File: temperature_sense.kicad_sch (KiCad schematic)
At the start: 1 part, among them U1 BQ79616PAPRQ1

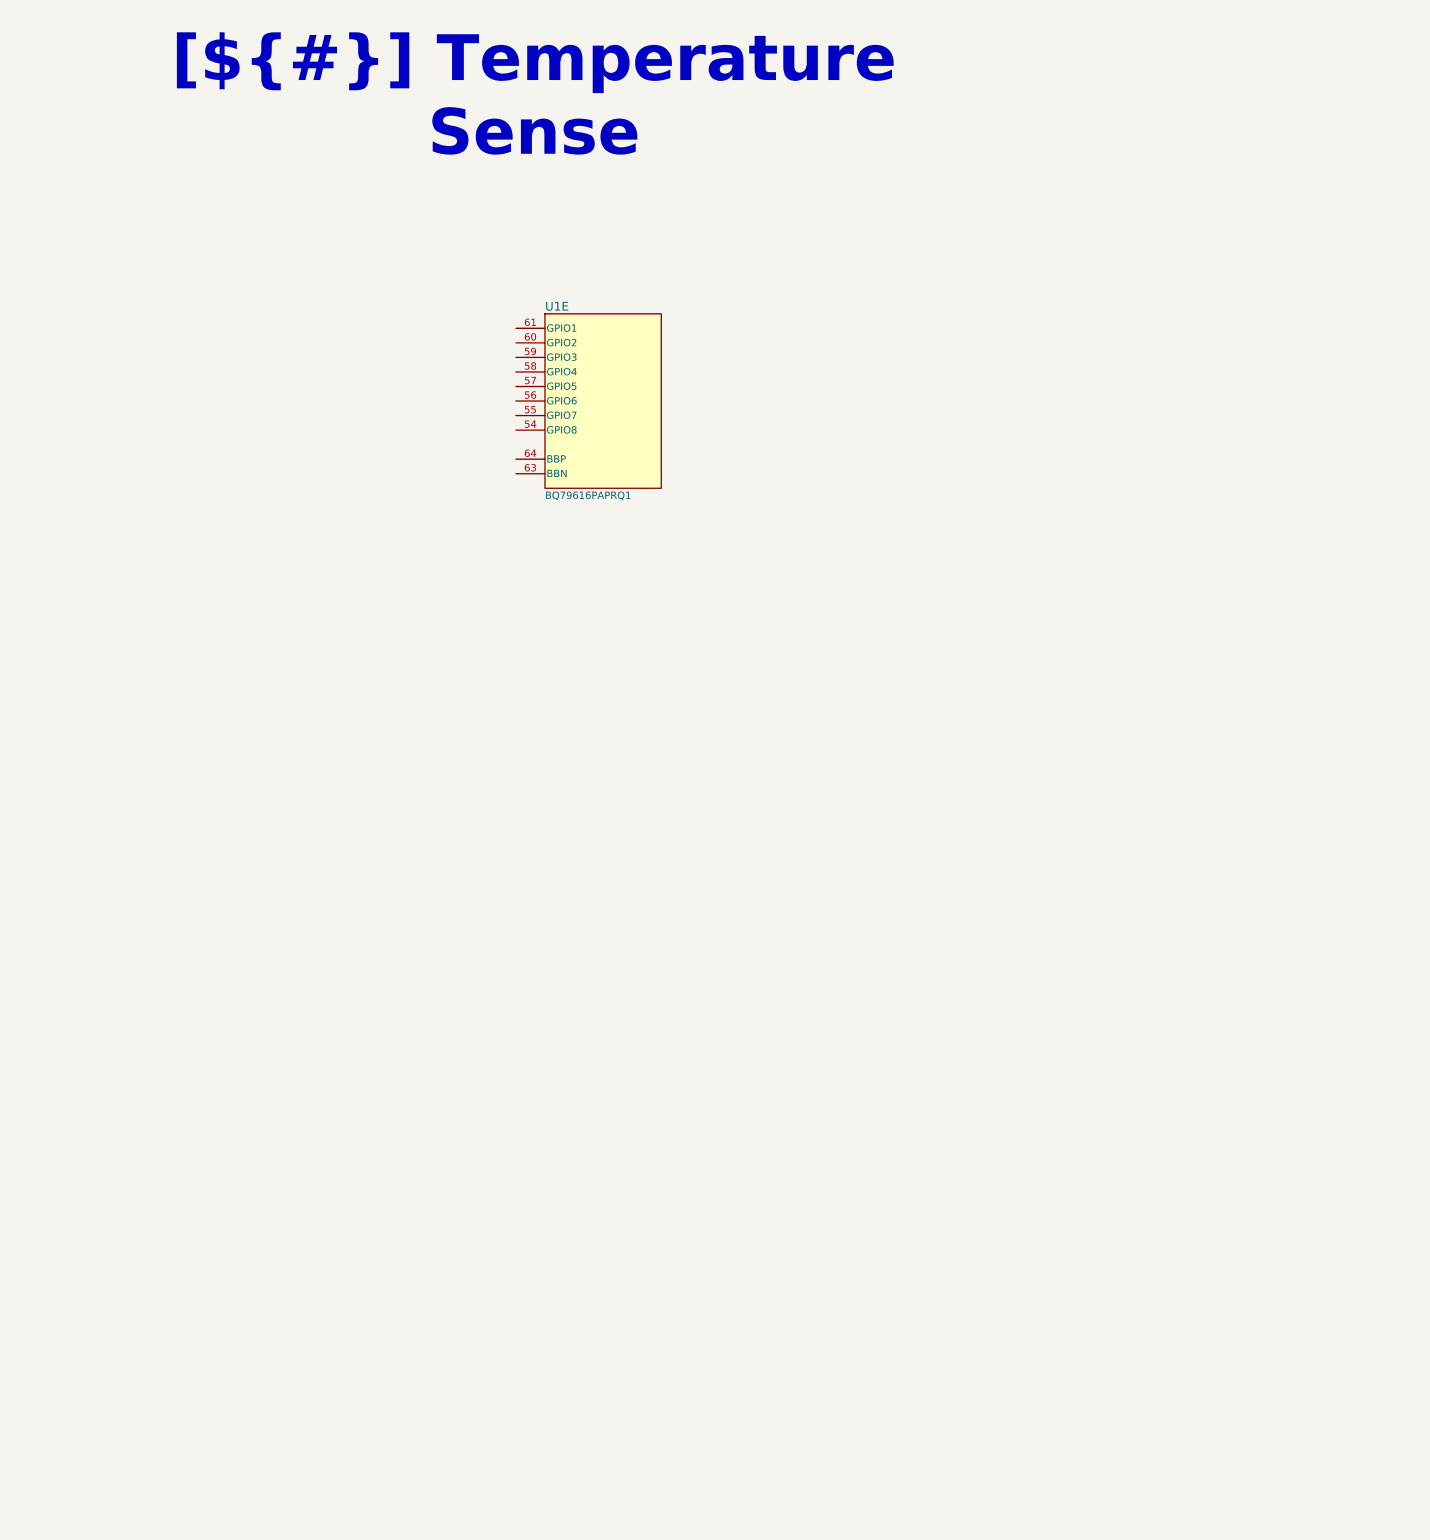
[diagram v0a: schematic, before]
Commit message: SCH:[Hiarchy, Temp, Power]:Inital schmatics of temp, balance, power mostly there need to add design notes and layout notes.
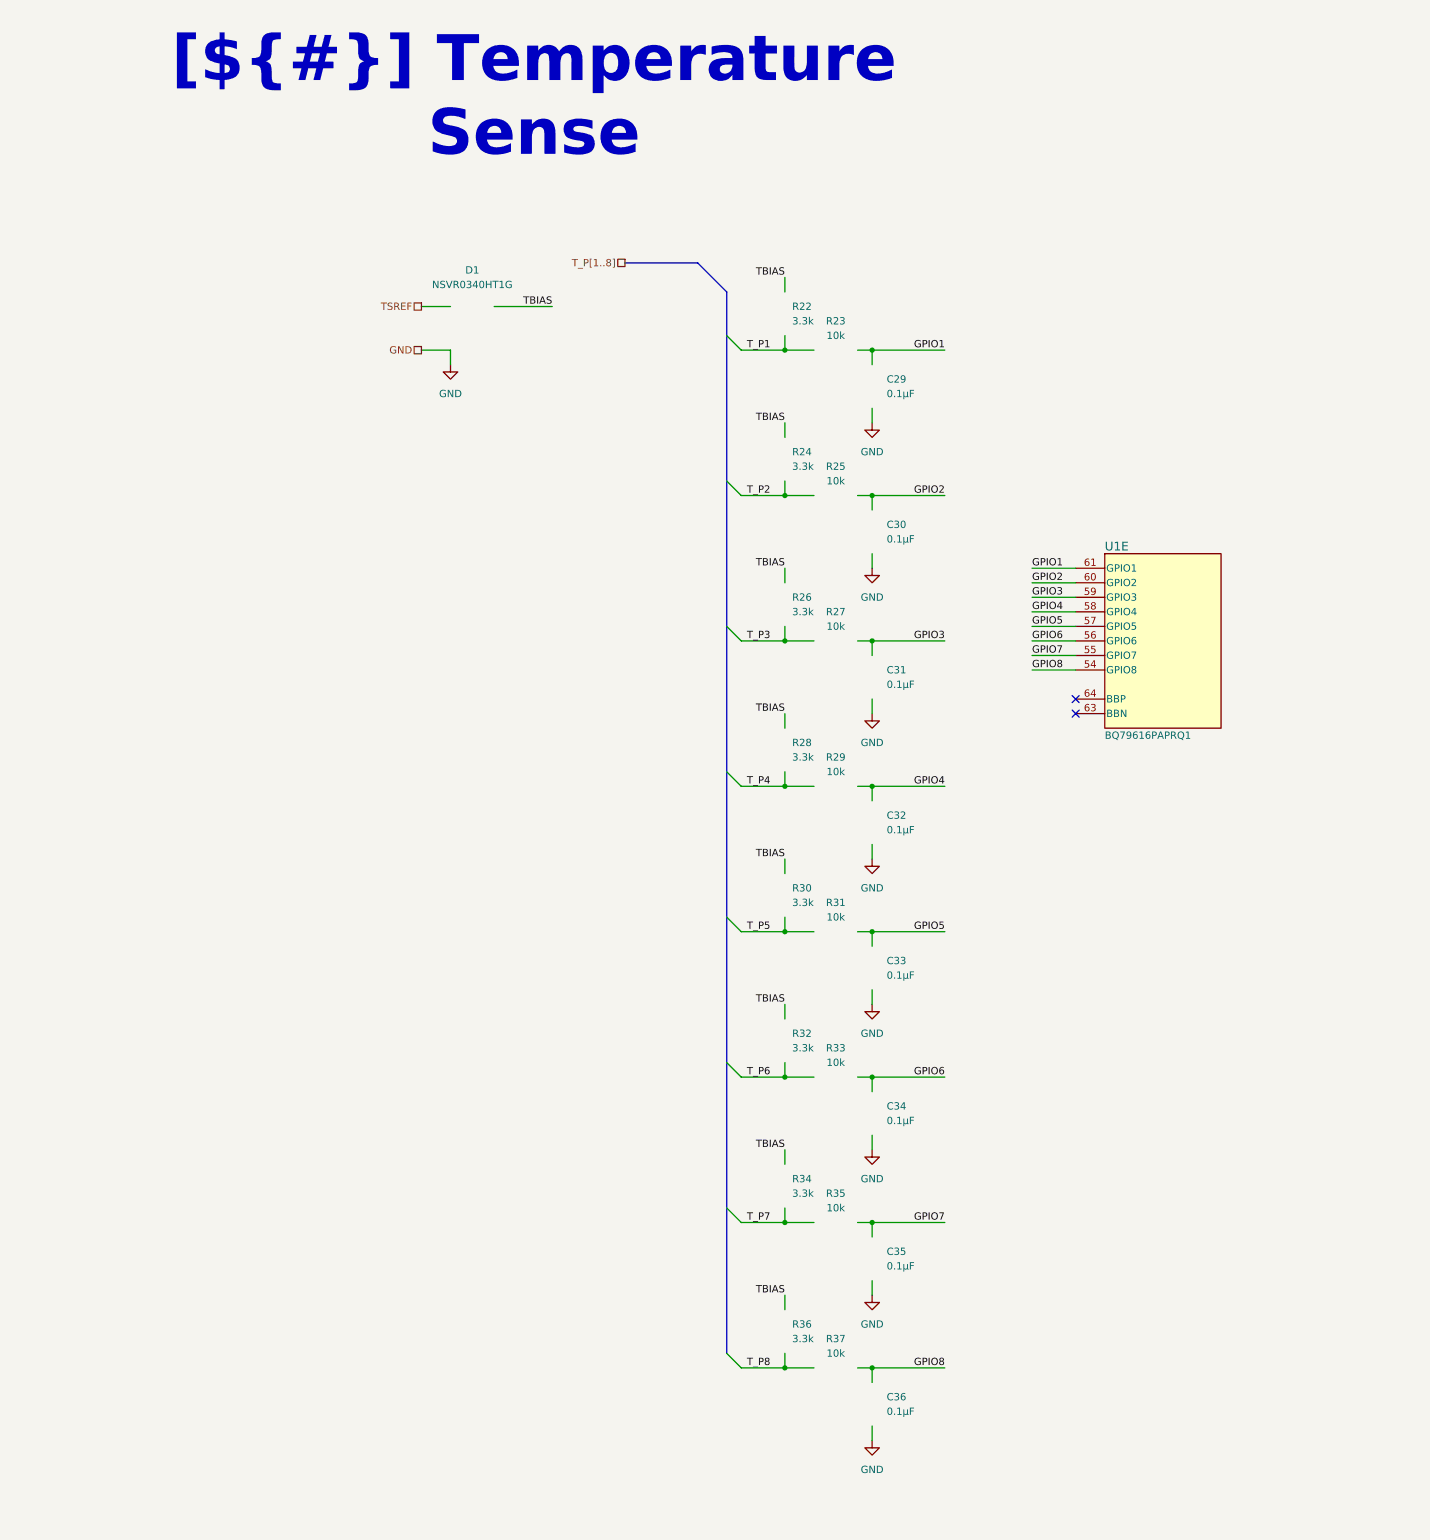
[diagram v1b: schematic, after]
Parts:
- added C29, C30, C31, C32, C33, C34, C35, C36: 0.1µF, remote_cl05a105ko5nnnc:C_0402_1005Metric, symbol remote_gcm155r71h104ke02j:C
- added D1: NSVR0340HT1G, remote_nsvr0340ht1g:SOD-323_1P7X1P25_ONS, symbol remote_nsvr0340ht1g:D
- added R22, R24, R26, R28, R30, R32, R34, R36: 3.3k, remote_rcs060359r0fkea:R_0603_1608Metric, symbol remote_erj-pa3f3301v:R_US
- added R23, R25, R27, R29, R31, R33, R35, R37: 10k, remote_erj-2ge0r00x:R_0402_1005Metric, symbol remote_erj-pa2f1002x:R_US
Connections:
- net GPIO8: now reaches U1.54 (GPIO8)
- net GPIO8: now also C36.1, R37.2
- net GPIO7: now reaches U1.55 (GPIO7)
- net GPIO7: now also C35.1, R35.2
- net GPIO6: now reaches U1.56 (GPIO6)
- net GPIO6: now also C34.1, R33.2
- net GPIO5: now reaches U1.57 (GPIO5)
- net GPIO5: now also C33.1, R31.2
- net GPIO4: now reaches U1.58 (GPIO4)
- net GPIO4: now also C32.1, R29.2
- net GPIO3: now reaches U1.59 (GPIO3)
- net GPIO3: now also C31.1, R27.2
- net GPIO2: now reaches U1.60 (GPIO2)
- net GPIO2: now also C30.1, R25.2
- net GPIO1: now reaches U1.61 (GPIO1)
- net GPIO1: now also C29.1, R23.2
- new net GND: C29.2, C30.2, C31.2, C32.2, C33.2, C34.2, C35.2, C36.2
- new net TBIAS: D1.1 (C), R22.1, R24.1, R26.1, R28.1, R30.1, R32.1, R34.1, R36.1
- new net TSREF: D1.2 (A)
- new net T_P1: R22.2, R23.1
- new net T_P2: R24.2, R25.1
- new net T_P3: R26.2, R27.1
- new net T_P4: R28.2, R29.1
- new net T_P5: R30.2, R31.1
- new net T_P6: R32.2, R33.1
- new net T_P7: R34.2, R35.1
- new net T_P8: R36.2, R37.1
- no-connect marks 0 -> 2
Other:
- moved on the sheet: U1E

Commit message: SCH: Schmatic is close to final, need to resolve a few ERC errors nothing major. Largest change will be adding seporate wires for VBAT and RefGround / Tap 0. connector position and types may change as mechaincal posision/layout is finalaized as well so holding off on layout for now.
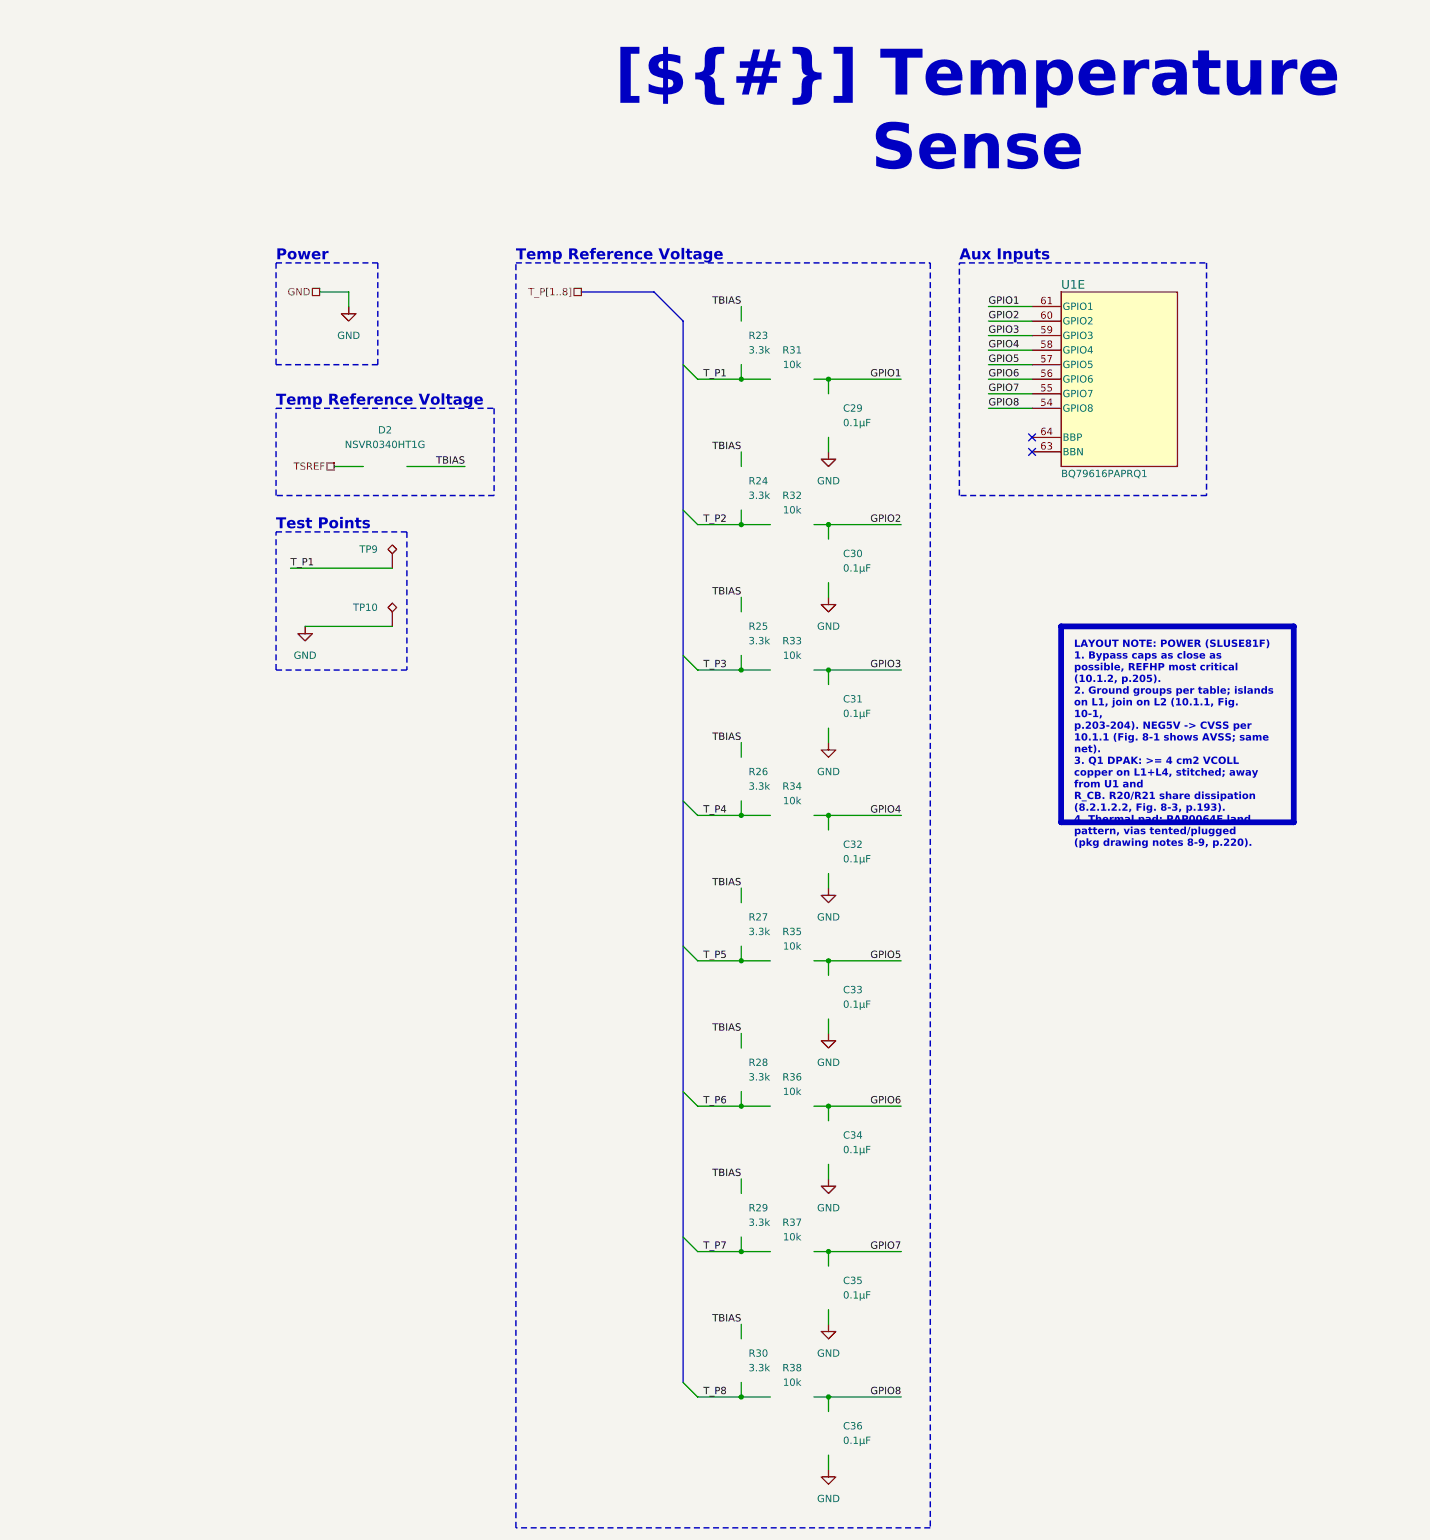
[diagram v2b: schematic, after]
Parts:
- removed D1: NSVR0340HT1G, remote_nsvr0340ht1g:SOD-323_1P7X1P25_ONS, symbol remote_nsvr0340ht1g:D
- added D2: NSVR0340HT1G, remote_nsvr0340ht1g:SOD-323_1P7X1P25_ONS, symbol remote_nsvr0340ht1g:D
- added TP10, TP9: (no value), TestPoint:TestPoint_Pad_D2.0mm, symbol Connector:TestPoint_Alt
- renumbered R22 to R23, R26 to R25, R28 to R26, R30 to R27, R32 to R28, R34 to R29, R36 to R30, R23 to R31, R25 to R32, R27 to R33, R29 to R34, R31 to R35, R33 to R36, R35 to R37, R37 to R38
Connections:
- net GND: now also TP10.1
- net TBIAS: now also D2.1 (C)
- net TSREF: now also D2.2 (A)
- net T_P1: now also TP9.1
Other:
- note added: "Aux Inputs"
- note added: "Power"
- note added: "Temp Reference Voltage"
- note added: "Test Points"
- moved on the sheet: U1E

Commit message: PCB[Mounting]: Messing with mounting holes for board to board connection. SCH[Naming]: Small naming changes, T_P -> TMP
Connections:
- net T_P1 renamed TMP1
- net T_P2 renamed TMP2
- net T_P3 renamed TMP3
- net T_P4 renamed TMP4
- net T_P5 renamed TMP5
- net T_P6 renamed TMP6
- net T_P7 renamed TMP7
- net T_P8 renamed TMP8
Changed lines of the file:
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@@
 	(text_box "LAYOUT NOTE: POWER (SLUSE81F)\n1. Bypass caps as close as possible, REFHP most critical (10.1.2, p.205).\n2. Ground groups per table; islands on L1, join on L2 (10.1.1, Fig. 10-1,\n   p.203-204). NEG5V -> CVSS per 10.1.1 (Fig. 8-1 shows AVSS; same net).\n3. Q1 DPAK: >= 4 cm2 VCOLL copper on L1+L4, stitched; away from U1 and\n   R_CB. R20/R21 share dissipation (8.2.1.2.2, Fig. 8-3, p.193).\n4. Thermal pad: PAP0064F land pattern, vias tented/plugged\n   (pkg drawing notes 8-9, p.220)."
 		(exclude_from_sim no)
-		(at 228.6 114.3 0)
+		(at 210.82 99.06 0)
 		(size 40.64 34.2268)
 		(margins 2.25 2.25 2.25 2.25)
@@
 		)
 	)
-	(label "T_P5"
+	(label "TMP5"
 		(at 170.18 172.72 180)
 		(fields_autoplaced yes)
@@
 		)
 	)
-	(label "T_P2"
+	(label "TMP2"
 		(at 170.18 96.52 180)
 		(fields_autoplaced yes)
@@
 		)
 	)
-	(label "T_P1"
+	(label "TMP1"
 		(at 170.18 71.12 180)
 		(fields_autoplaced yes)
@@
 		)
 	)
-	(label "T_P7"
+	(label "TMP7"
 		(at 170.18 223.52 180)
-		(effects
-			(font
-				(size 1.27 1.27)
-			)
-			(justify right bottom)
-		)
-	)
-	(label "T_P1"
+		(fields_autoplaced yes)
+		(effects
+			(font
+				(size 1.27 1.27)
+			)
+			(justify right bottom)
+		)
+		(property "Netclass" "TEMP"
+			(at 170.18 224.79 0)
+			(show_name no)
+			(do_not_autoplace no)
+			(effects
+				(font
+					(size 1.27 1.27)
+					(italic yes)
+				)
+				(justify right)
+			)
+		)
+	)
+	(label "TMP1"
 		(at 93.98 104.14 0)
 		(fields_autoplaced yes)
@@
 		)
 	)
-	(label "T_P6"
+	(label "TMP6"
 		(at 170.18 198.12 180)
 		(fields_autoplaced yes)
@@
 		)
 	)
-	(label "T_P3"
+	(label "TMP3"
 		(at 170.18 121.92 180)
 		(fields_autoplaced yes)
@@
 		)
 	)
-	(label "T_P4"
+	(label "TMP4"
 		(at 170.18 147.32 180)
 		(fields_autoplaced yes)
@@
 		)
 	)
-	(label "T_P8"
+	(label "TMP8"
 		(at 170.18 248.92 180)
-		(effects
-			(font
-				(size 1.27 1.27)
-			)
-			(justify right bottom)
+		(fields_autoplaced yes)
+		(effects
+			(font
+				(size 1.27 1.27)
+			)
+			(justify right bottom)
+		)
+		(property "Netclass" "TEMP"
+			(at 170.18 250.19 0)
+			(show_name no)
+			(do_not_autoplace no)
+			(effects
+				(font
+					(size 1.27 1.27)
+					(italic yes)
+				)
+				(justify right)
+			)
 		)
 	)
@@
 		)
 	)
-	(hierarchical_label "T_P[1..8]"
+	(hierarchical_label "TMP[1..8]"
 		(shape passive)
 		(at 144.78 55.88 180)

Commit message: PCB[Test Points, Mechanical, Silk]: Finalized Mounting Points, Added Testpoints with adjecent silkscreen labels. SCH[Test Points, Notes]: Added/Updated notes for all pages, cleaned up errors spelling ect.
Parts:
- removed TP10, TP9: (no value), TestPoint:TestPoint_Pad_D2.0mm, symbol Connector:TestPoint_Alt
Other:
- note added: "Sensor Bias & RC Filter (x8)"
- note removed: "Test Points"

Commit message: PCB[Trace Size, Testpad, Daisy]: Changed Bat Trace size FAT, Made test pads larger, small trace movement to clean up, daisy trace change. SCH[Notes]: Small notes changes.
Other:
- company: (none) -> ${COMPANY}
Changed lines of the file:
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@@
 	(title_block
 		(title "Temperature Sense")
+		(date "2026-10-28")
+		(rev "${REVISION}")
+		(company "${COMPANY}")
 	)
 	(rectangle
